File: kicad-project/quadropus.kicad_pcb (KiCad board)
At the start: 2 copper layers, 50 x 50 mm, 42 parts, among them J1 USB-C_HRO_31-M-12, J2 Conn_01x05, J3 Conn_01x05, J4 Conn_01x05, J5 Conn_01x05, U1 CP2108-B03-GM

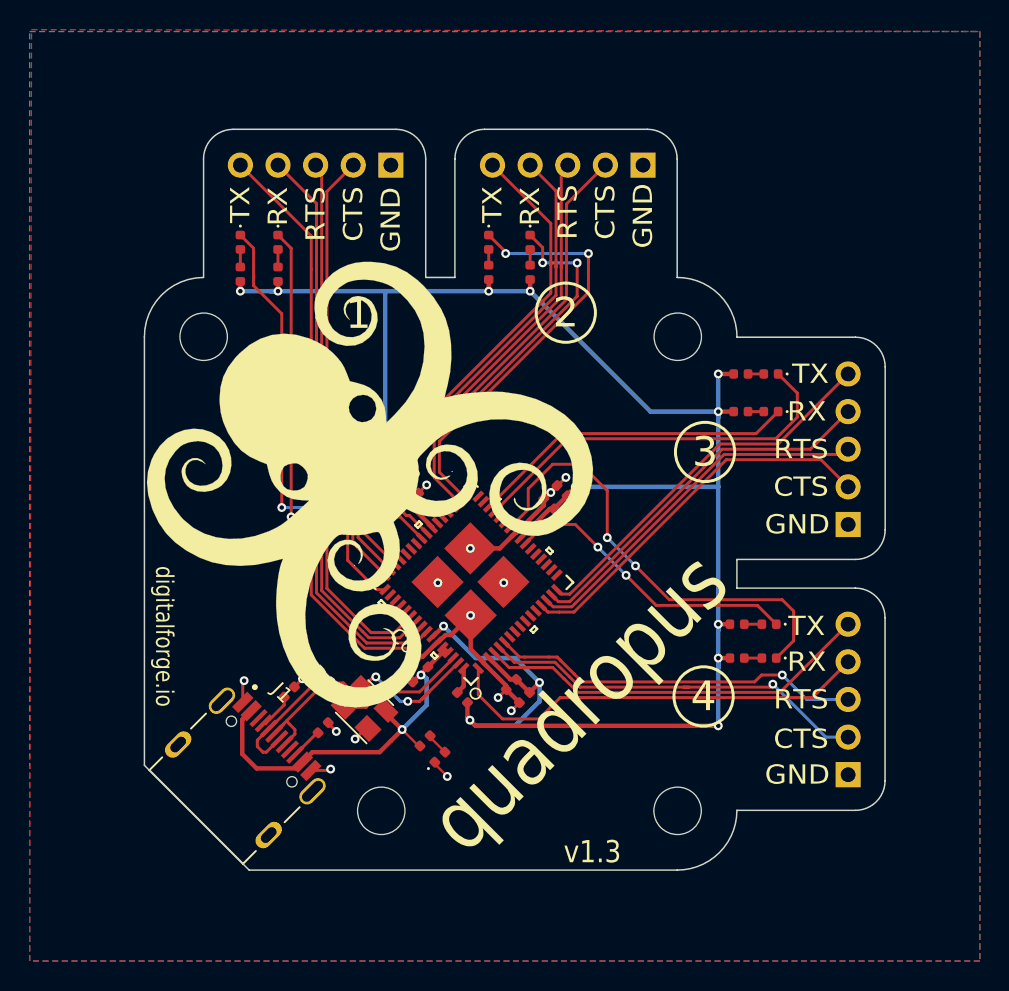
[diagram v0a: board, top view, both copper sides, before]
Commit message: Swap TX/RX LEDs
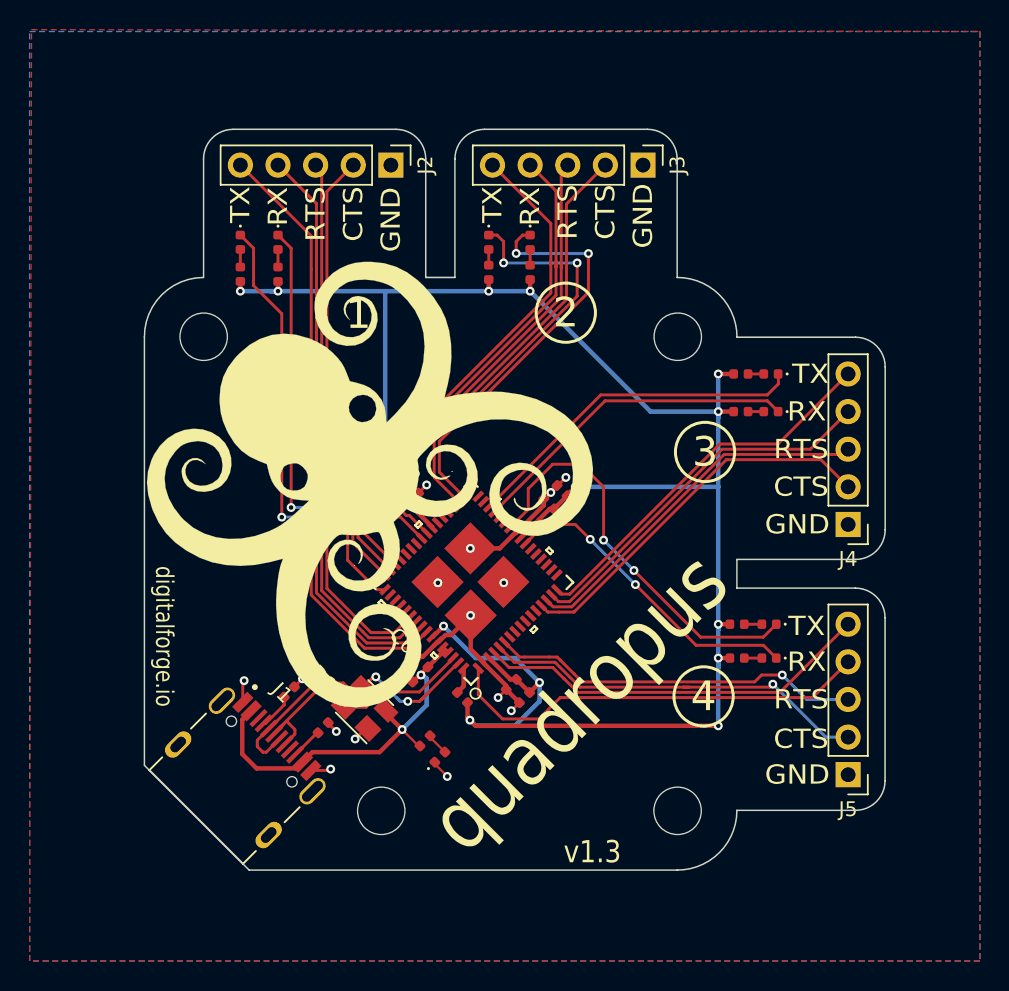
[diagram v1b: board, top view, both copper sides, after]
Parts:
- J2, J3, J4, J5: footprint Connector_PinHeader_2.54mm:PinHeader_1x05_P2.54mm_NO-SILK -> Connector_PinHeader_2.54mm:PinHeader_1x05_P2.54mm_Vertical
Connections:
- D2 pad 1: /GPIO_0 -> /GPIO_1
- D3 pad 1: /GPIO_4 -> /GPIO_5
- D4 pad 1: /GPIO_8 -> /GPIO_9
- D5 pad 1: /GPIO_12 -> /GPIO_13
- D6 pad 1: /GPIO_1 -> /GPIO_0
- D7 pad 1: /GPIO_5 -> /GPIO_4
- D8 pad 1: /GPIO_9 -> /GPIO_8
- D9 pad 1: /GPIO_13 -> /GPIO_12
- J1 pad A8: (no net) -> Net-(J1-PadA8)
- J1 pad B8: (no net) -> Net-(J1-PadB8)
- U1 pad 10: (no net) -> Net-(U1-Pad10)
- U1 pad 11: (no net) -> Net-(U1-Pad11)
- U1 pad 12: (no net) -> Net-(U1-Pad12)
- U1 pad 17: (no net) -> Net-(U1-Pad17)
- U1 pad 18: (no net) -> Net-(U1-Pad18)
- U1 pad 19: (no net) -> Net-(U1-Pad19)
- U1 pad 20: (no net) -> Net-(U1-Pad20)
- U1 pad 21: (no net) -> Net-(U1-Pad21)
- U1 pad 22: (no net) -> Net-(U1-Pad22)
- U1 pad 27: (no net) -> Net-(U1-Pad27)
- U1 pad 28: (no net) -> Net-(U1-Pad28)
- U1 pad 31: (no net) -> Net-(U1-Pad31)
- U1 pad 32: (no net) -> Net-(U1-Pad32)
- U1 pad 35: (no net) -> Net-(U1-Pad35)
- U1 pad 36: (no net) -> Net-(U1-Pad36)
- U1 pad 37: (no net) -> Net-(U1-Pad37)
- U1 pad 38: (no net) -> Net-(U1-Pad38)
- U1 pad 42: (no net) -> Net-(U1-Pad42)
- U1 pad 43: (no net) -> Net-(U1-Pad43)
- U1 pad 44: (no net) -> Net-(U1-Pad44)
- U1 pad 45: (no net) -> Net-(U1-Pad45)
- U1 pad 50: (no net) -> Net-(U1-Pad50)
- U1 pad 51: (no net) -> Net-(U1-Pad51)
- U1 pad 52: (no net) -> Net-(U1-Pad52)
- U1 pad 53: (no net) -> Net-(U1-Pad53)
- U1 pad 7: (no net) -> Net-(U1-Pad7)
- U1 pad 8: (no net) -> Net-(U1-Pad8)
- U1 pad 9: (no net) -> Net-(U1-Pad9)
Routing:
- net /GPIO_9: track 26.6 -> 22.6 mm
- net /GPIO_12: track 31.4 -> 27.9 mm
- net /GPIO_4: track 25.3 -> 28.4 mm
- net /GPIO_8: track 22.2 -> 23.7 mm
- net /GPIO_0: track 28.8 -> 30.2 mm
- net /GPIO_1: track 30.1 -> 28.7 mm
- net /GPIO_13: track 20.3 -> 21.2 mm
